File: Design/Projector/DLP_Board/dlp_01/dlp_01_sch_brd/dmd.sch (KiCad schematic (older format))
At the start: 0 parts

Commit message: Ongoing updates the schematics
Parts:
- added U? (x4): DLP3310AFQM, symbol TexasInstruments_DLP:DLP3310AFQM
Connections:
- new net +1V8: U?.A19 (VDD_2), U?.A20 (VDD_3), U?.A21 (VDD_4), U?.B19 (VDDI_2), U?.B20 (VDD_5), U?.B6 (VDDI_1), U?.C2 (VDD_6), U?.C23 (VDDI_4), U?.C3 (VDDI_3), U?.D2 (VDD_7), U?.D23 (VDD_9), U?.D3 (VDD_8), U?.E2 (VDD_10), U?.E23 (VDDI_6), U?.E3 (VDDI_5), U?.F2 (VDD_11), U?.F23 (VDD_13), U?.F3 (VDD_12), U?.G23 (VDDI_8), U?.G3 (VDDI_7)
- new net DMD_DEN_ARSTZ: U?.B2 (DMD_DEN_ARSTZ)
- new net DMD_LS_CLK: U?.B5 (LS_CLK)
- new net DMD_LS_RDATA: U?.B7 (LS_RDATA_A)
- new net DMD_LS_WDATA: U?.B3 (LS_WDATA)
- new net GND: U?.A2 (VSS_1), U?.A24 (VSS_5), U?.A3 (VSS_2), U?.A4 (VSS_3), U?.A7 (VSS_4), U?.B22 (VSS_6), U?.B23 (VSS_7), U?.B24 (VSS_8), U?.C19 (VSS_11), U?.C22 (VSS_12), U?.C4 (VSS_9), U?.C7 (VSS_10), U?.E19 (VSS_15), U?.E22 (VSS_16), U?.E4 (VSS_13), U?.E7 (VSS_14), U?.G19 (VSS_19), U?.G22 (VSS_20), U?.G24 (VSS_21), U?.G4 (VSS_17), U?.G7 (VSS_18), U?.H2 (VSS_22), U?.H23 (VSS_24), U?.H24 (VSS_25), U?.H3 (VSS_23)
- new net VBIAS: U?.A22 (VBIAS[2]), U?.A6 (VBIAS[2])
- new net VOFFSET: U?.B21 (VOFFSET[2]), U?.G2 (VOFFSET[2])
- new net VRESET: U?.A23 (VRESET[2]), U?.A5 (VRESET[2])
- new net mDMD_HS_CLK_N: U?.E6 (DCLK_AN)
- new net mDMD_HS_CLK_P: U?.E5 (DCLK_AP)
- new net mDMD_HS_WDATAA_N: U?.F7 (D_AN(3))
- new net mDMD_HS_WDATAA_P: U?.F6 (D_AP(3))
- new net mDMD_HS_WDATAB_N: U?.D5 (D_AN(2))
- new net mDMD_HS_WDATAB_P: U?.D4 (D_AP(2))
- new net mDMD_HS_WDATAC_N: U?.D7 (D_AN(1))
- new net mDMD_HS_WDATAC_P: U?.D6 (D_AP(1))
- new net mDMD_HS_WDATAD_N: U?.C6 (D_AN(0))
- new net mDMD_HS_WDATAD_P: U?.C5 (D_AP(0))
- new net mDMD_HS_WDATAE_N: U?.H7 (D_AN(7))
- new net mDMD_HS_WDATAE_P: U?.H6 (D_AP(7))
- new net mDMD_HS_WDATAF_N: U?.H5 (D_AN(6))
- new net mDMD_HS_WDATAF_P: U?.H4 (D_AP(6))
- new net mDMD_HS_WDATAG_N: U?.G6 (D_AN(5))
- new net mDMD_HS_WDATAG_P: U?.G5 (D_AP(5))
- new net mDMD_HS_WDATAH_N: U?.F5 (D_AN(4))
- new net mDMD_HS_WDATAH_P: U?.F4 (D_AP(4))
- new net sDMD_HS_CLK_N: U?.E20 (DCLK_BN)
- new net sDMD_HS_CLK_P: U?.E21 (DCLK_BP)
- new net sDMD_HS_WDATAA_N: U?.F21 (D_BN(4))
- new net sDMD_HS_WDATAA_P: U?.F22 (D_BP(4))
- new net sDMD_HS_WDATAB_N: U?.G20 (D_BN(5))
- new net sDMD_HS_WDATAB_P: U?.G21 (D_BP(5))
- new net sDMD_HS_WDATAC_N: U?.H21 (D_BN(6))
- new net sDMD_HS_WDATAC_P: U?.H22 (D_BP(6))
- new net sDMD_HS_WDATAD_N: U?.H19 (D_BN(7))
- new net sDMD_HS_WDATAD_P: U?.H20 (D_BP(7))
- new net sDMD_HS_WDATAE_N: U?.C20 (D_BN(0))
- new net sDMD_HS_WDATAE_P: U?.C21 (D_BP(0))
- new net sDMD_HS_WDATAF_N: U?.D19 (D_BN(1))
- new net sDMD_HS_WDATAF_P: U?.D20 (D_BP(1))
- new net sDMD_HS_WDATAG_N: U?.D21 (D_BN(2))
- new net sDMD_HS_WDATAG_P: U?.D22 (D_BP(2))
- new net sDMD_HS_WDATAH_N: U?.F19 (D_BN(3))
- new net sDMD_HS_WDATAH_P: U?.F20 (D_BP(3))
- new net sDMD_LS_RDATA: U?.B4 (LS_RDATA_B)

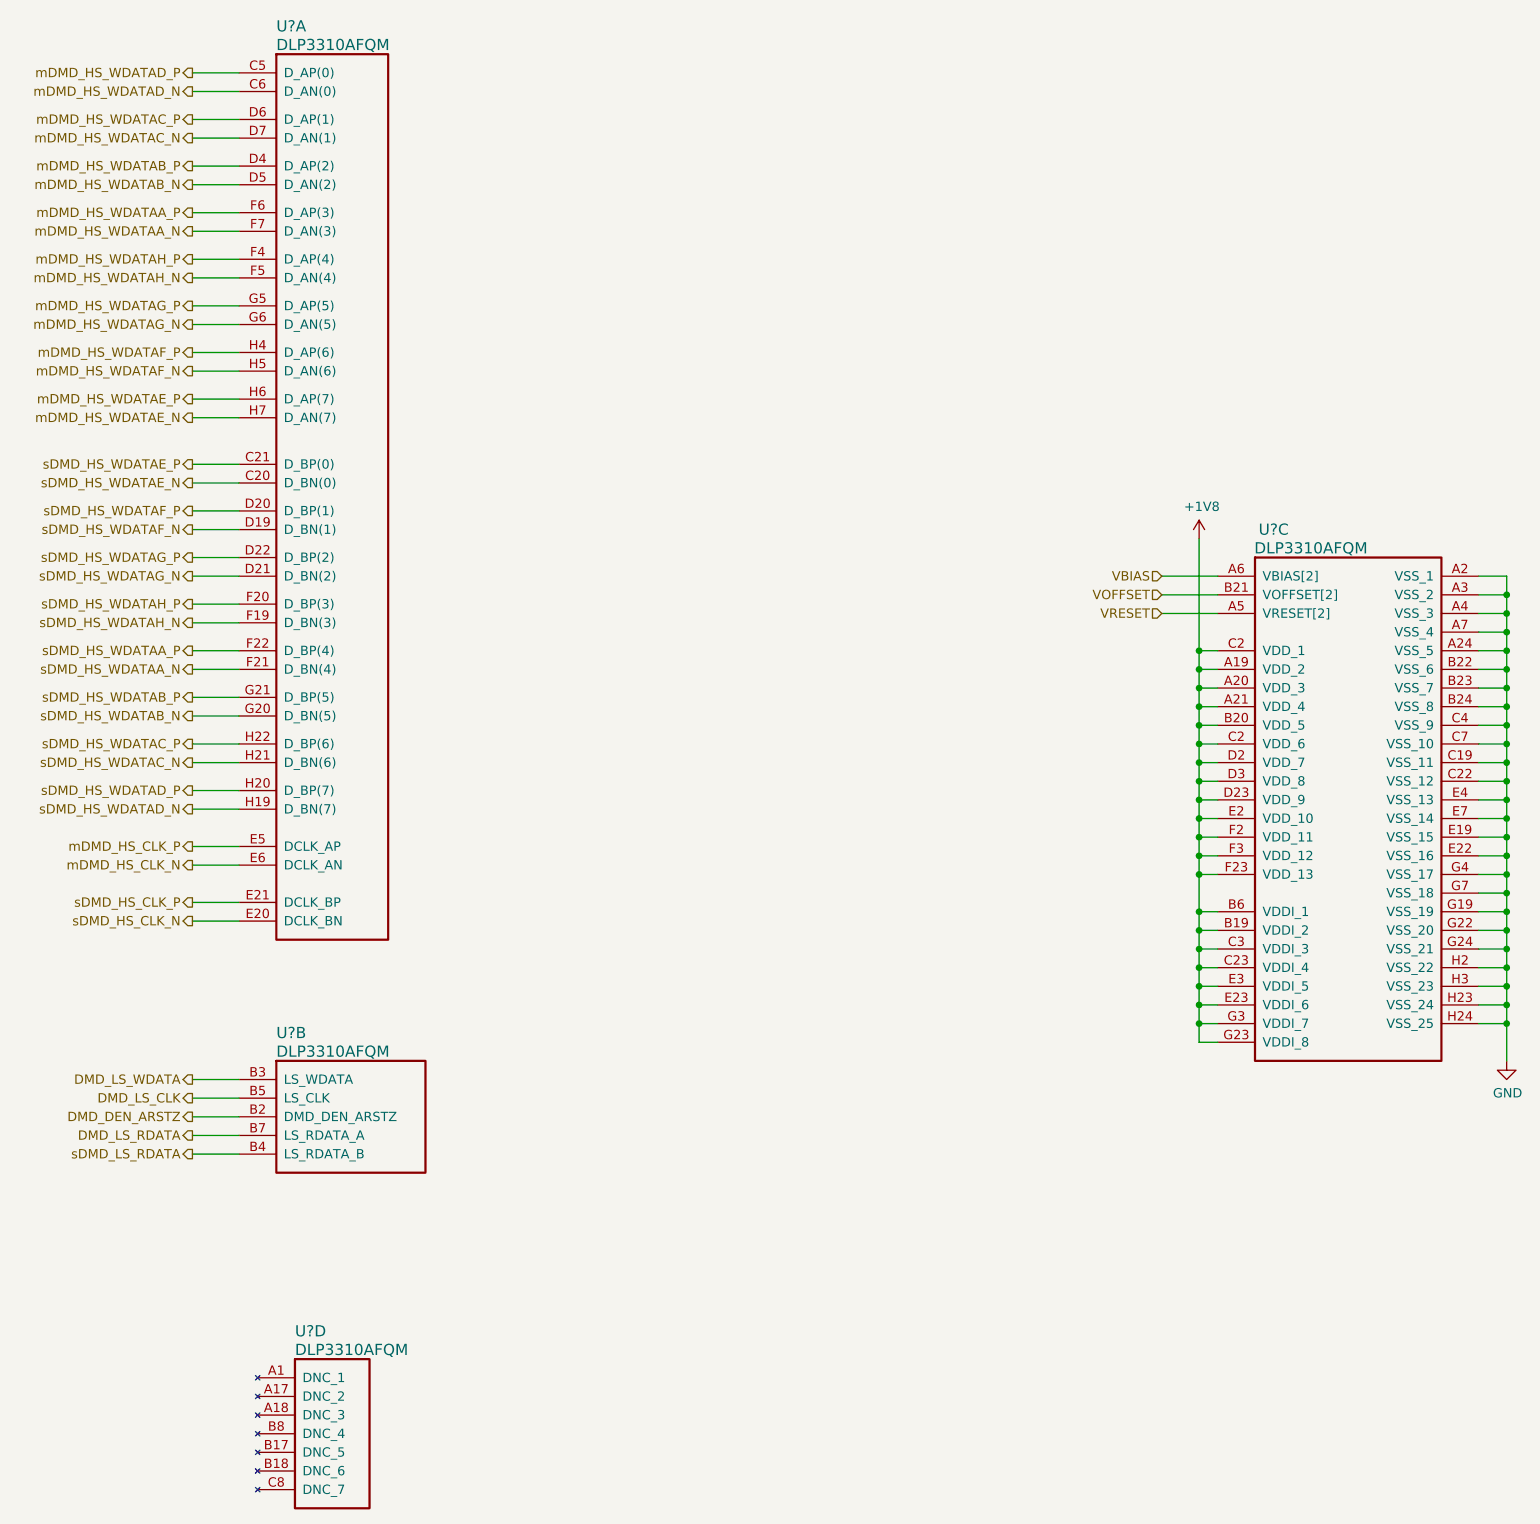
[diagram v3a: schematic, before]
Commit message: Initial placement of power converters, BGA fanout and Z-turn board outline imported
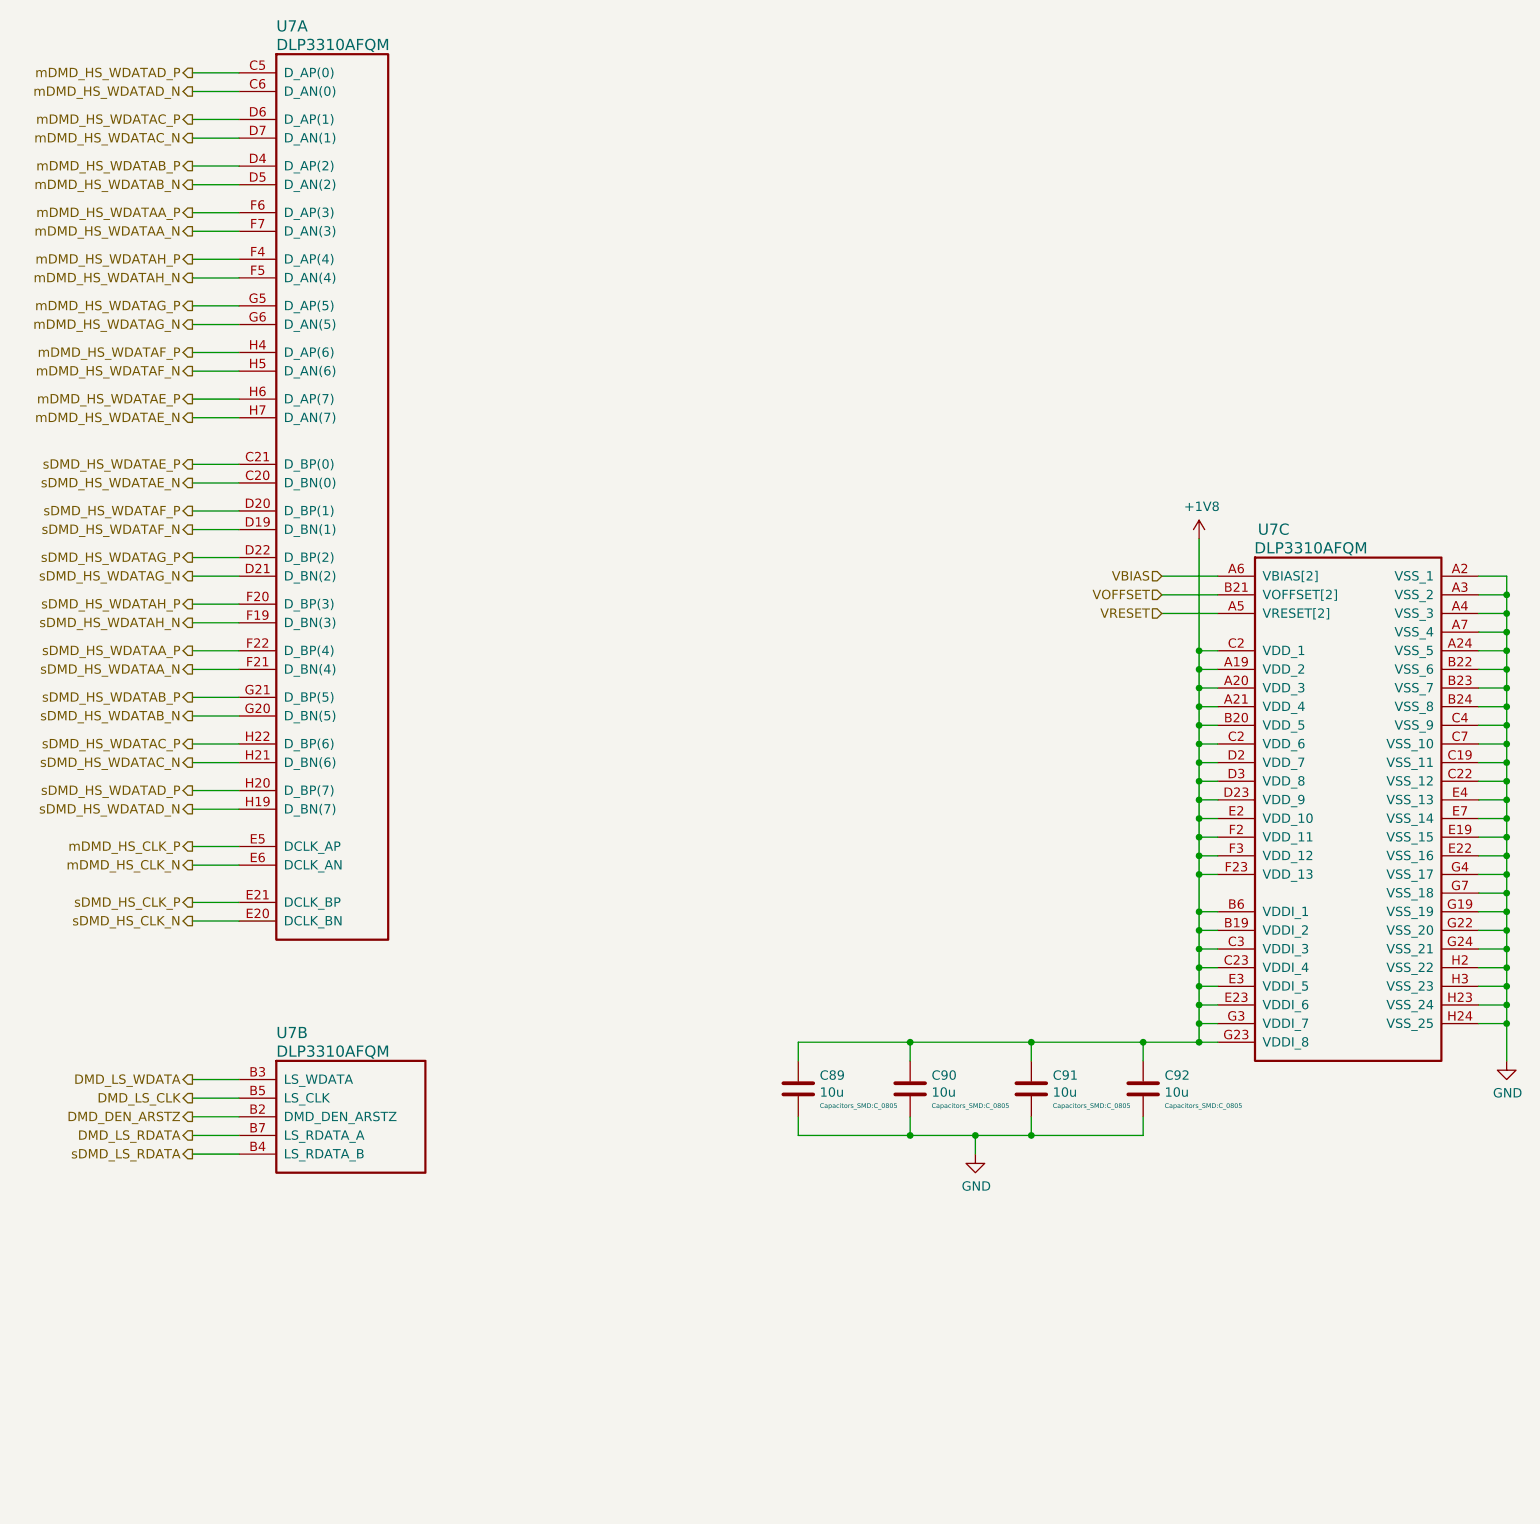
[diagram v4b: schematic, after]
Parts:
- removed U?: DLP3310AFQM, symbol TexasInstruments_DLP:DLP3310AFQM
- added C89, C90, C91, C92: 10u, Capacitors_SMD:C_0805, symbol Device:C
- U7: renamed from U?; footprint (none) -> DLP3310:DLP3310
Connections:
- net +1V8: now also C89.1, C90.1, C91.1, C92.1
- net GND: now also C89.2, C90.2, C91.2, C92.2
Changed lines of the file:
@@
 $Descr A3 16535 11693
 encoding utf-8
-Sheet 9 10
+Sheet 9 11
 Title ""
 Date ""
@@
 $EndDescr
 $Comp
-L TexasInstruments_DLP:DLP3310AFQM U?
+L TexasInstruments_DLP:DLP3310AFQM U7
 U 1 1 5D2CE3FC
 P 5400 1950
-F 0 "U?" H 5600 2200 60  0000 L CNN
+F 0 "U7" H 5600 2200 60  0000 L CNN
 F 1 "DLP3310AFQM" H 5600 2100 60  0000 L CNN
-F 2 "" H 5400 1950 50  0001 C CNN
+F 2 "DLP3310:DLP3310" H 5400 1950 50  0001 C CNN
 F 3 "http://www.ti.com/lit/ds/symlink/dlp3310.pdf" H 5400 1950 50  0001 C CNN
 	1    5400 1950
@@
 $EndComp
 $Comp
-L TexasInstruments_DLP:DLP3310AFQM U?
+L TexasInstruments_DLP:DLP3310AFQM U7
 U 2 1 5D2D07D4
 P 5400 7350
-F 0 "U?" H 5600 7600 60  0000 L CNN
+F 0 "U7" H 5600 7600 60  0000 L CNN
 F 1 "DLP3310AFQM" H 5600 7500 60  0000 L CNN
-F 2 "" H 5400 7350 50  0001 C CNN
+F 2 "DLP3310:DLP3310" H 5400 7350 50  0001 C CNN
 F 3 "http://www.ti.com/lit/ds/symlink/dlp3310.pdf" H 5400 7350 50  0001 C CNN
 	2    5400 7350
@@
 $EndComp
 $Comp
-L TexasInstruments_DLP:DLP3310AFQM U?
+L TexasInstruments_DLP:DLP3310AFQM U7
 U 3 1 5D2D4583
 P 10650 4650
-F 0 "U?" H 10950 4900 60  0000 C CNN
+F 0 "U7" H 10950 4900 60  0000 C CNN
 F 1 "DLP3310AFQM" H 11150 4800 60  0000 C CNN
-F 2 "" H 10650 4650 50  0001 C CNN
+F 2 "DLP3310:DLP3310" H 10650 4650 50  0001 C CNN
 F 3 "http://www.ti.com/lit/ds/symlink/dlp3310.pdf" H 10650 4650 50  0001 C CNN
 	3    10650 4650
@@
 $EndComp
 $Comp
-L TexasInstruments_DLP:DLP3310AFQM U?
-U 4 1 5D2D7439
-P 5500 8950
-F 0 "U?" H 5700 9200 60  0000 L CNN
-F 1 "DLP3310AFQM" H 5700 9100 60  0000 L CNN
-F 2 "" H 5500 8950 50  0001 C CNN
-F 3 "http://www.ti.com/lit/ds/symlink/dlp3310.pdf" H 5500 8950 50  0001 C CNN
-	4    5500 8950
-	1    0    0    -1
-$EndComp
-$Comp
-L power:GND #PWR?
+L power:GND #PWR0102
 U 1 1 5D2E1967
 P 12200 7250
-F 0 "#PWR?" H 12200 7000 50  0001 C CNN
+F 0 "#PWR0102" H 12200 7000 50  0001 C CNN
 F 1 "GND" H 12205 7077 50  0000 C CNN
 F 2 "" H 12200 7250 50  0001 C CNN
@@
 P 10550 4450
 AR Path="/5D712001/5D3077C6" Ref="#PWR?"  Part="1"
-AR Path="/5EBD88DC/5D3077C6" Ref="#PWR?"  Part="1"
-F 0 "#PWR?" H 10550 4300 50  0001 C CNN
+AR Path="/5EBD88DC/5D3077C6" Ref="#PWR0101"  Part="1"
+F 0 "#PWR0101" H 10550 4300 50  0001 C CNN
 F 1 "+1V8" H 10565 4623 50  0000 C CNN
 F 2 "" H 10550 4450 50  0001 C CNN
@@
 Wire Wire Line
 	5400 7550 5150 7550
+$Comp
+L Device:C C92
+U 1 1 5D4E31E1
+P 10250 7400
+F 0 "C92" H 10365 7472 50  0000 L CNN
+F 1 "10u" H 10365 7381 50  0000 L CNN
+F 2 "Capacitors_SMD:C_0805" H 10365 7309 25  0000 L CNN
+F 3 "~" H 10250 7400 50  0001 C CNN
+	1    10250 7400
+	1    0    0    -1
+$EndComp
+$Comp
+L Device:C C91
+U 1 1 5D4F02C5
+P 9650 7400
+F 0 "C91" H 9765 7472 50  0000 L CNN
+F 1 "10u" H 9765 7381 50  0000 L CNN
+F 2 "Capacitors_SMD:C_0805" H 9765 7309 25  0000 L CNN
+F 3 "~" H 9650 7400 50  0001 C CNN
+	1    9650 7400
+	1    0    0    -1
+$EndComp
+$Comp
+L Device:C C90
+U 1 1 5D4F2EDA
+P 9000 7400
+F 0 "C90" H 9115 7472 50  0000 L CNN
+F 1 "10u" H 9115 7381 50  0000 L CNN
+F 2 "Capacitors_SMD:C_0805" H 9115 7309 25  0000 L CNN
+F 3 "~" H 9000 7400 50  0001 C CNN
+	1    9000 7400
+	1    0    0    -1
+$EndComp
+$Comp
+L Device:C C89
+U 1 1 5D4F2EE0
+P 8400 7400
+F 0 "C89" H 8515 7472 50  0000 L CNN
+F 1 "10u" H 8515 7381 50  0000 L CNN
+F 2 "Capacitors_SMD:C_0805" H 8515 7309 25  0000 L CNN
+F 3 "~" H 8400 7400 50  0001 C CNN
+	1    8400 7400
+	1    0    0    -1
+$EndComp
+$Comp
+L power:GND #PWR0100
+U 1 1 5D4F981C
+P 9350 7750
+F 0 "#PWR0100" H 9350 7500 50  0001 C CNN
+F 1 "GND" H 9355 7577 50  0000 C CNN
+F 2 "" H 9350 7750 50  0001 C CNN
+F 3 "" H 9350 7750 50  0001 C CNN
+	1    9350 7750
+	1    0    0    -1
+$EndComp
+Wire Wire Line
+	10550 7150 10250 7150
+Wire Wire Line
+	8400 7150 8400 7250
+Connection ~ 10550 7150
+Wire Wire Line
+	9000 7250 9000 7150
+Connection ~ 9000 7150
+Wire Wire Line
+	9000 7150 8400 7150
+Wire Wire Line
+	9650 7250 9650 7150
+Connection ~ 9650 7150
+Wire Wire Line
+	9650 7150 9000 7150
+Wire Wire Line
+	10250 7250 10250 7150
+Connection ~ 10250 7150
+Wire Wire Line
+	10250 7150 9650 7150
+Wire Wire Line
+	10250 7550 10250 7650
+Wire Wire Line
+	10250 7650 9650 7650
+Wire Wire Line
+	8400 7650 8400 7550
+Wire Wire Line
+	9000 7550 9000 7650
+Connection ~ 9000 7650
+Wire Wire Line
+	9000 7650 8400 7650
+Wire Wire Line
+	9650 7550 9650 7650
+Connection ~ 9650 7650
+Wire Wire Line
+	9350 7750 9350 7650
+Connection ~ 9350 7650
+Wire Wire Line
+	9350 7650 9000 7650
+Wire Wire Line
+	9350 7650 9650 7650
 $EndSCHEMATC
